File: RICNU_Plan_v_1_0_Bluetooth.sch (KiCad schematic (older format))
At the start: 6 parts, among them SW2 SW_Push, U7 BT121

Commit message: Re-routed CAN, RS-485, and debug connectors (wrong polarity in all)
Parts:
- removed SW2: SW_Push, Buttons_Switches_SMD:SW_SPST_KMR2, symbol SW_Push
- added SW2: SW_Push_4pin, RICNU_Plan_v_1_0:SW_SPST_KMR7, symbol SW_Push_4pin
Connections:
- no-connect marks 20 -> 22
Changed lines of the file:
@@
-$EndComp
-$Comp
-L SW_Push SW2
-U 1 1 59FAF2AD
-P 6900 4500
-F 0 "SW2" H 6950 4600 50  0000 L CNN
-F 1 "SW_Push" H 6900 4440 50  0000 C CNN
-F 2 "Buttons_Switches_SMD:SW_SPST_KMR2" H 6900 4700 50  0001 C CNN
-F 3 "" H 6900 4700 50  0001 C CNN
-	1    6900 4500
-	0    1    1    0
 $EndComp
 $Comp
@@
 Text Label 7100 3450 0    60   ~ 0
 BT_VCC
+$Comp
+L SW_Push_4pin SW2
+U 1 1 5A1F72AC
+P 6900 4500
+F 0 "SW2" H 6950 4600 50  0000 L CNN
+F 1 "SW_Push_4pin" V 7300 4300 50  0001 C CNN
+F 2 "RICNU_Plan_v_1_0:SW_SPST_KMR7" H 6900 4700 50  0001 C CNN
+F 3 "" H 6900 4700 50  0001 C CNN
+	1    6900 4500
+	0    1    1    0
+$EndComp
+NoConn ~ 6800 4300
+NoConn ~ 6800 4700
 $EndSCHEMATC

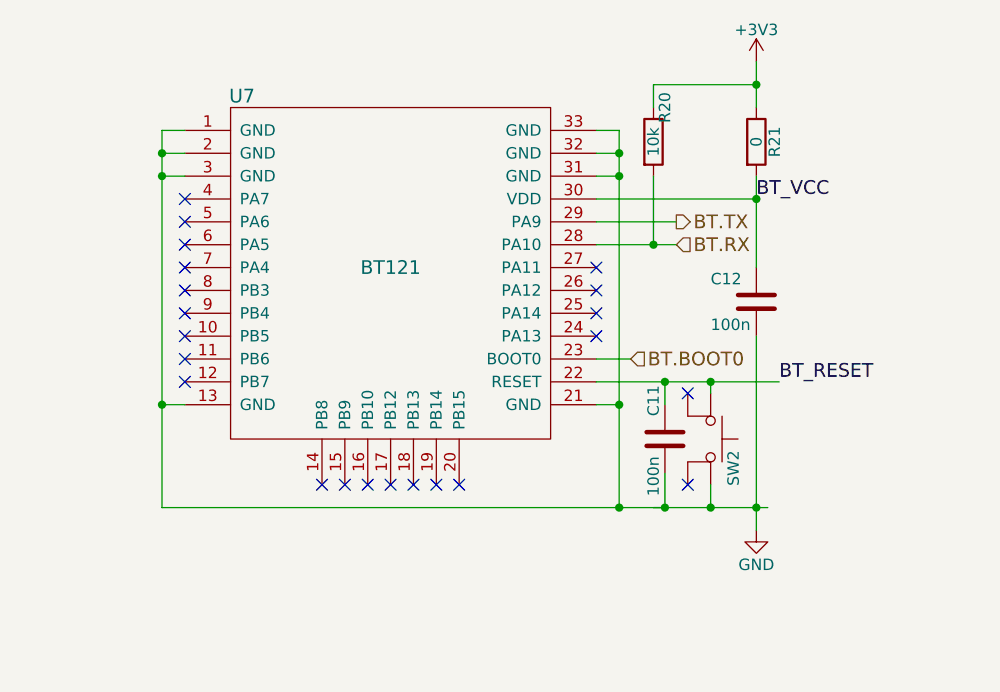
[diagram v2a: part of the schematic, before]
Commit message: Various small changes like comment removal
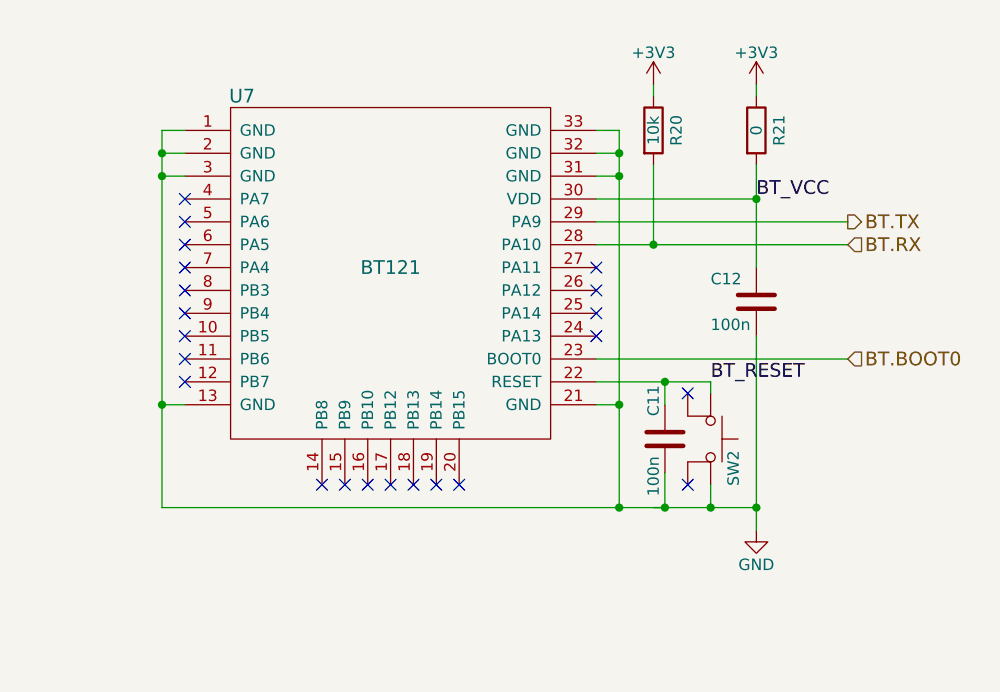
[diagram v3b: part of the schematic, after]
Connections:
- wire segments 27 -> 39
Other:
- moved on the sheet: R20, R21
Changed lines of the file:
@@
 	1    0    0    -1
 $EndComp
-Text HLabel 6550 4150 2    60   Input ~ 0
+Text HLabel 7500 4150 2    60   Input ~ 0
 BT.BOOT0
 $Comp
@@
 	1    0    0    -1
 $EndComp
-Text HLabel 6750 3650 2    60   Input ~ 0
+Text HLabel 7500 3650 2    60   Input ~ 0
 BT.RX
-Text HLabel 6750 3550 2    60   Output ~ 0
+Text HLabel 7500 3550 2    60   Output ~ 0
 BT.TX
 $Comp
 L +3V3 #PWR040
 U 1 1 59FDDC6B
-P 7100 2850
-F 0 "#PWR040" H 7100 2700 50  0001 C CNN
-F 1 "+3V3" H 7100 2990 50  0000 C CNN
-F 2 "" H 7100 2850 50  0001 C CNN
-F 3 "" H 7100 2850 50  0001 C CNN
-	1    7100 2850
+P 7100 2950
+F 0 "#PWR040" H 7100 2800 50  0001 C CNN
+F 1 "+3V3" H 7100 3090 50  0000 C CNN
+F 2 "" H 7100 2950 50  0001 C CNN
+F 3 "" H 7100 2950 50  0001 C CNN
+	1    7100 2950
 	1    0    0    -1
 $EndComp
@@
 L R R21
 U 1 1 59F5F953
-P 7100 3200
-F 0 "R21" V 7180 3200 50  0000 C CNN
-F 1 "0" V 7100 3200 50  0000 C CNN
-F 2 "Resistors_SMD:R_0402_NoSilk" V 7030 3200 50  0001 C CNN
-F 3 "" H 7100 3200 50  0001 C CNN
-	1    7100 3200
+P 7100 3150
+F 0 "R21" V 7200 3150 50  0000 C CNN
+F 1 "0" V 7100 3150 50  0000 C CNN
+F 2 "Resistors_SMD:R_0402_NoSilk" V 7030 3150 50  0001 C CNN
+F 3 "" H 7100 3150 50  0001 C CNN
+	1    7100 3150
 	1    0    0    -1
 $EndComp
@@
 	6900 4800 6900 4700
 Wire Wire Line
-	4500 4800 7150 4800
+	4500 4800 6500 4800
+Wire Wire Line
+	6500 4800 6700 4800
+Wire Wire Line
+	6700 4800 6900 4800
+Wire Wire Line
+	6900 4800 7100 4800
 Wire Wire Line
 	6700 4800 6650 4800
 Connection ~ 6900 4800
-Wire Wire Line
-	6900 4250 6900 4300
 Wire Wire Line
 	6700 4650 6700 4800
@@
 NoConn ~ 5800 4700
 Wire Wire Line
-	4500 3150 4500 4800
+	4500 3150 4500 3250
+Wire Wire Line
+	4500 3250 4500 3350
+Wire Wire Line
+	4500 3350 4500 4350
+Wire Wire Line
+	4500 4350 4500 4800
 Wire Wire Line
 	4500 4350 4600 4350
@@
 	6500 4350 6400 4350
 Wire Wire Line
-	6500 3150 6500 4800
+	6500 3150 6500 3250
+Wire Wire Line
+	6500 3250 6500 3350
+Wire Wire Line
+	6500 3350 6500 4350
+Wire Wire Line
+	6500 4350 6500 4800
 Wire Wire Line
 	6400 3150 6500 3150
@@
 	6400 3450 7100 3450
 Wire Wire Line
-	7100 3350 7100 3750
+	7100 3300 7100 3450
+Wire Wire Line
+	7100 3450 7100 3750
 $Comp
 L GND #PWR041
@@
 $EndComp
 Wire Wire Line
-	7100 4050 7100 4900
+	7100 4050 7100 4800
+Wire Wire Line
+	7100 4800 7100 4900
 Connection ~ 7100 3450
 Wire Wire Line
-	7100 2850 7100 3050
+	7100 2950 7100 3000
 $Comp
 L R R20
 U 1 1 59FBEA73
-P 6650 3200
-F 0 "R20" V 6700 3350 50  0000 C CNN
-F 1 "10k" V 6650 3200 50  0000 C CNN
-F 2 "Resistors_SMD:R_0402_NoSilk" V 6580 3200 50  0001 C CNN
-F 3 "" H 6650 3200 50  0001 C CNN
-	1    6650 3200
-	1    0    0    -1
-$EndComp
-Wire Wire Line
-	6400 3650 6750 3650
-Wire Wire Line
-	6650 3650 6650 3350
+P 6650 3150
+F 0 "R20" V 6750 3150 50  0000 C CNN
+F 1 "10k" V 6650 3150 50  0000 C CNN
+F 2 "Resistors_SMD:R_0402_NoSilk" V 6580 3150 50  0001 C CNN
+F 3 "" H 6650 3150 50  0001 C CNN
+	1    6650 3150
+	1    0    0    -1
+$EndComp
+Wire Wire Line
+	6400 3650 6650 3650
+Wire Wire Line
+	6650 3650 7500 3650
+Wire Wire Line
+	6650 3650 6650 3300
 Connection ~ 7100 4800
 Wire Wire Line
-	6650 3050 6650 2950
-Wire Wire Line
-	6650 2950 7100 2950
-Connection ~ 7100 2950
-Wire Wire Line
-	6400 3550 6750 3550
+	6650 2950 6650 3000
+Wire Wire Line
+	6400 3550 7500 3550
 Connection ~ 6650 3650
 NoConn ~ 4600 3450
@@
 NoConn ~ 6400 3750
 Wire Wire Line
-	6550 4150 6400 4150
-Wire Wire Line
-	6400 4250 7200 4250
-Text Label 7200 4250 0    60   ~ 0
+	7500 4150 6400 4150
+Wire Wire Line
+	6400 4250 6700 4250
+Wire Wire Line
+	6700 4250 6900 4250
+Text Label 6900 4250 0    60   ~ 0
 BT_RESET
-Connection ~ 6900 4250
 Text Label 7100 3450 0    60   ~ 0
 BT_VCC
@@
 NoConn ~ 6800 4300
 NoConn ~ 6800 4700
+Wire Wire Line
+	6900 4250 6900 4300
+$Comp
+L +3V3 #PWR?
+U 1 1 5A70F686
+P 6650 2950
+F 0 "#PWR?" H 6650 2800 50  0001 C CNN
+F 1 "+3V3" H 6650 3090 50  0000 C CNN
+F 2 "" H 6650 2950 50  0001 C CNN
+F 3 "" H 6650 2950 50  0001 C CNN
+	1    6650 2950
+	1    0    0    -1
+$EndComp
 $EndSCHEMATC

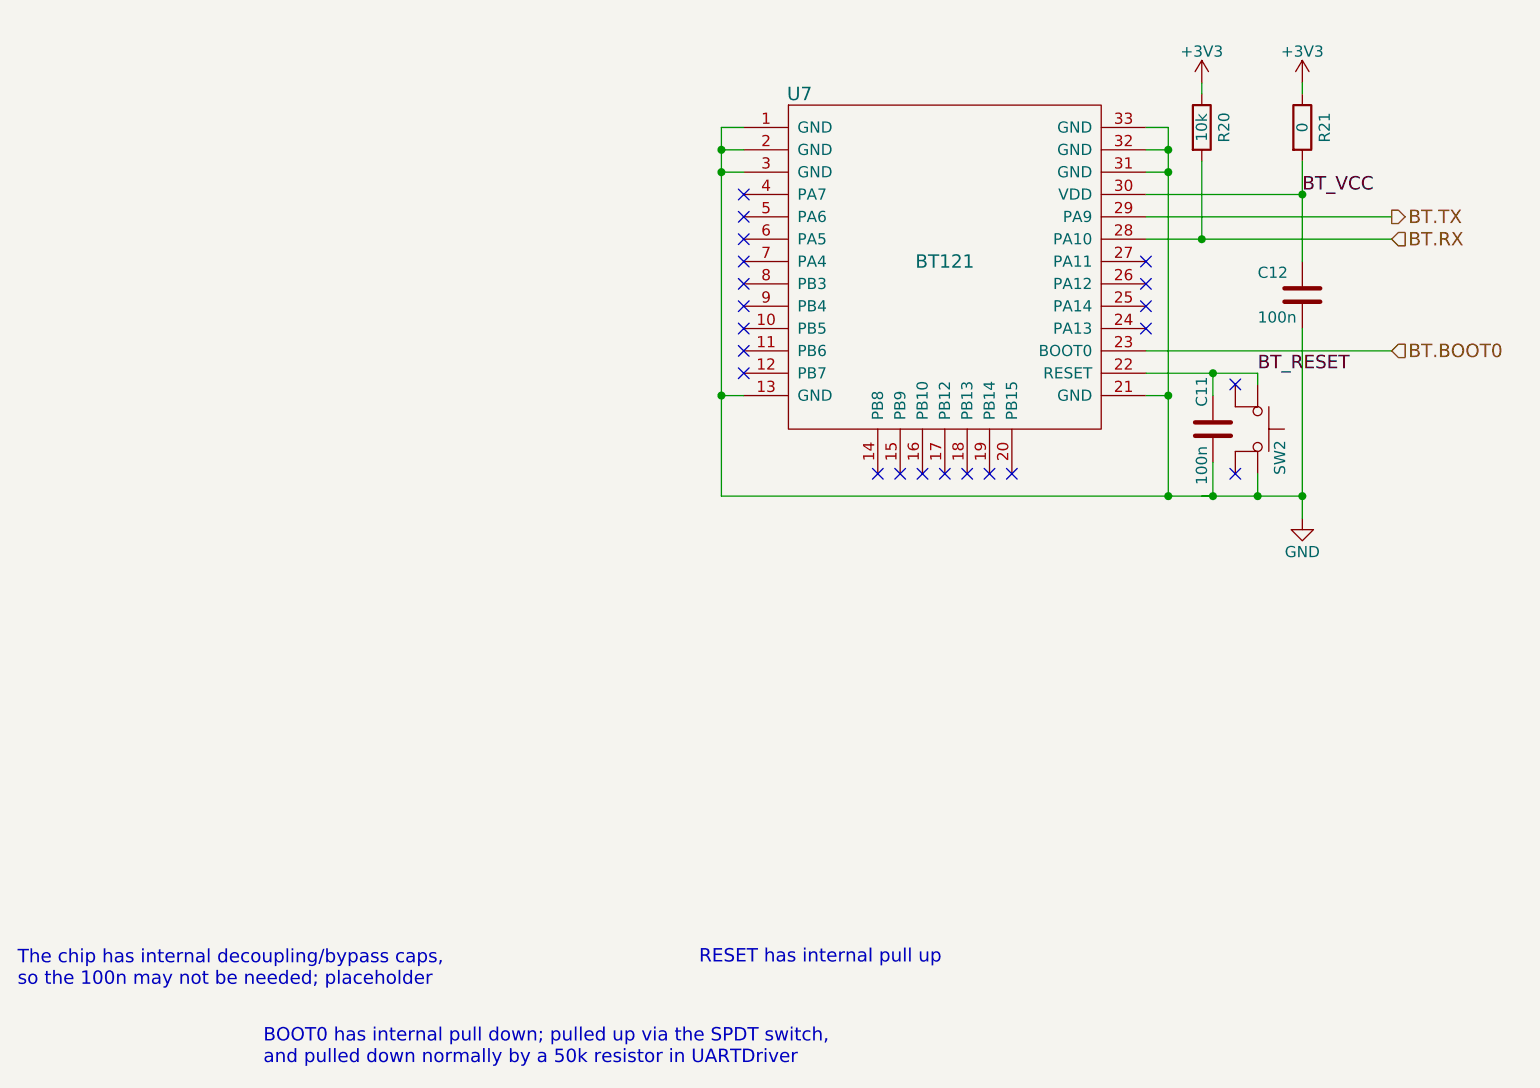
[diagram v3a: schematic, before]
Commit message: Deleting PDFs
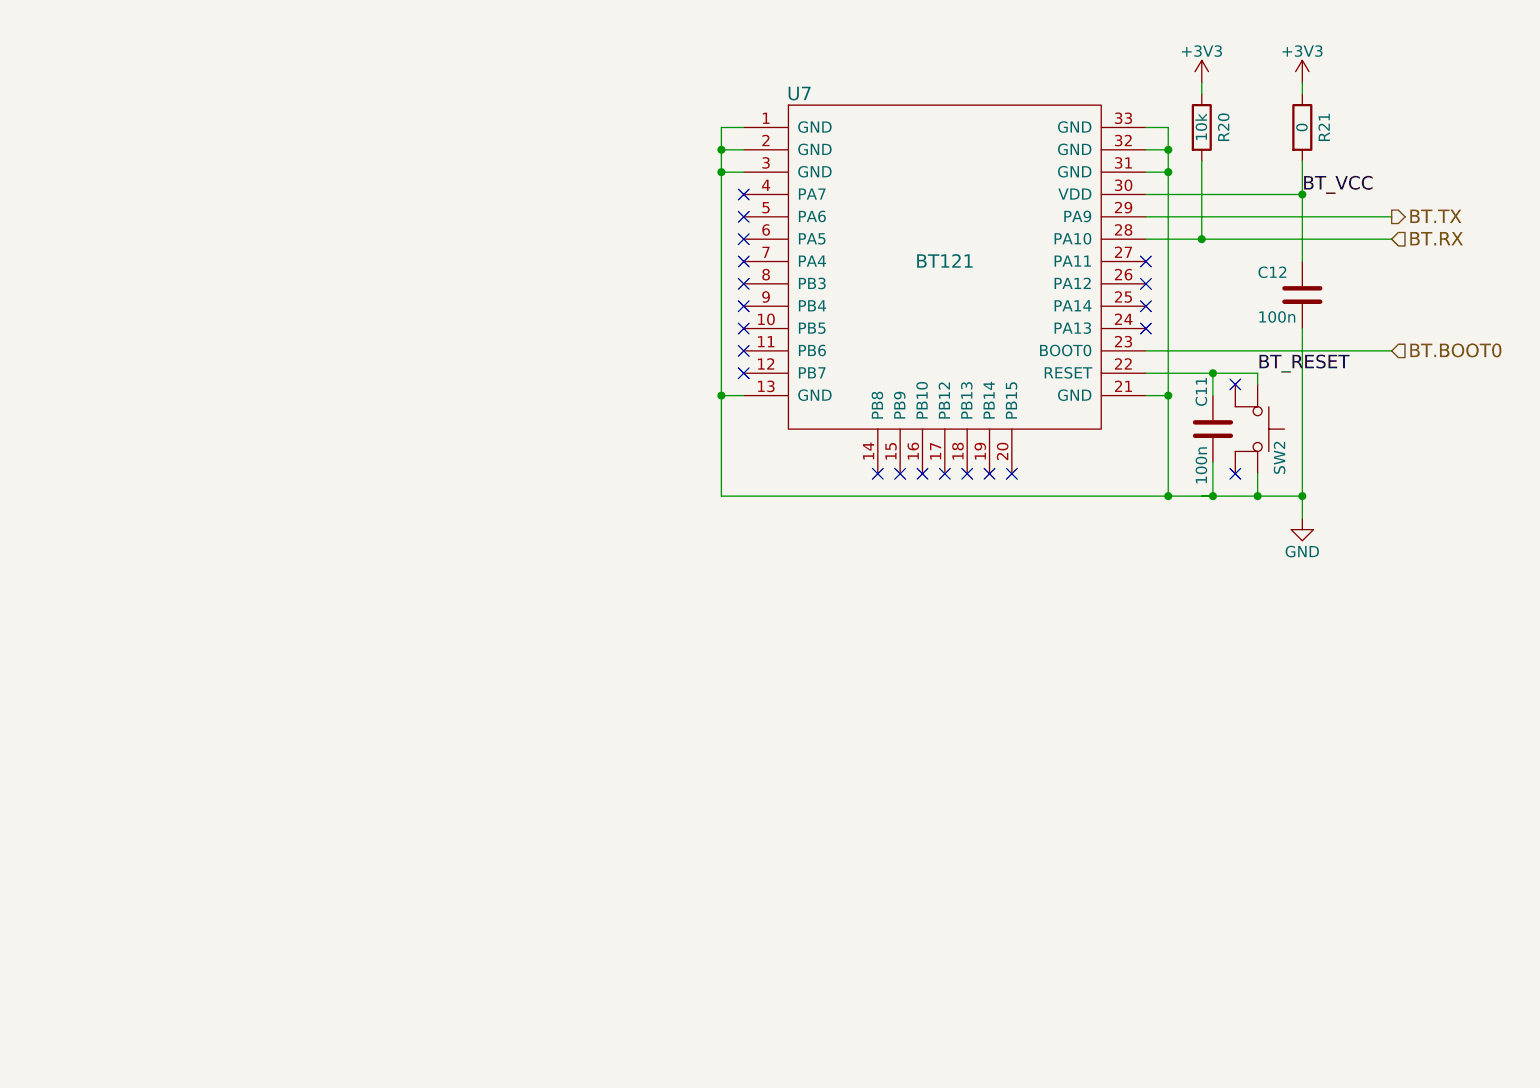
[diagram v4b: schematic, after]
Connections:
- wire segments 39 -> 26
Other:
- note removed: "BOOT0 has internal pull down; pulled up via the SPDT switch, \nand pulled down normally by a 50k resistor in UARTDriver"
- note removed: "RESET has internal pull up"
- note removed: "The chip has internal decoupling/bypass caps, \nso the 100n may not be needed; placeholder"
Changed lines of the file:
@@
 	1    0    0    -1
 $EndComp
-Text Notes 2450 7350 0    60   ~ 0
-BOOT0 has internal pull down; pulled up via the SPDT switch, \nand pulled down normally by a 50k resistor in UARTDriver
-Text Notes 4400 6900 0    60   ~ 0
-RESET has internal pull up
-Text Notes 1350 7000 0    60   ~ 0
-The chip has internal decoupling/bypass caps, \nso the 100n may not be needed; placeholder
 $Comp
 L R R21
@@
 	6900 4800 6900 4700
 Wire Wire Line
-	4500 4800 6500 4800
-Wire Wire Line
-	6500 4800 6700 4800
-Wire Wire Line
-	6700 4800 6900 4800
-Wire Wire Line
-	6900 4800 7100 4800
+	4500 4800 7100 4800
 Wire Wire Line
 	6700 4800 6650 4800
@@
 NoConn ~ 5800 4700
 Wire Wire Line
-	4500 3150 4500 3250
-Wire Wire Line
-	4500 3250 4500 3350
-Wire Wire Line
-	4500 3350 4500 4350
-Wire Wire Line
-	4500 4350 4500 4800
+	4500 3150 4500 4800
 Wire Wire Line
 	4500 4350 4600 4350
@@
 	6500 4350 6400 4350
 Wire Wire Line
-	6500 3150 6500 3250
-Wire Wire Line
-	6500 3250 6500 3350
-Wire Wire Line
-	6500 3350 6500 4350
-Wire Wire Line
-	6500 4350 6500 4800
+	6500 3150 6500 4800
 Wire Wire Line
 	6400 3150 6500 3150
@@
 	6400 3450 7100 3450
 Wire Wire Line
-	7100 3300 7100 3450
-Wire Wire Line
-	7100 3450 7100 3750
+	7100 3300 7100 3750
 $Comp
 L GND #PWR041
@@
 $EndComp
 Wire Wire Line
-	7100 4050 7100 4800
-Wire Wire Line
-	7100 4800 7100 4900
+	7100 4050 7100 4900
 Connection ~ 7100 3450
 Wire Wire Line
@@
 $EndComp
 Wire Wire Line
-	6400 3650 6650 3650
-Wire Wire Line
-	6650 3650 7500 3650
+	6400 3650 7500 3650
 Wire Wire Line
 	6650 3650 6650 3300
@@
 	7500 4150 6400 4150
 Wire Wire Line
-	6400 4250 6700 4250
-Wire Wire Line
-	6700 4250 6900 4250
+	6400 4250 6900 4250
 Text Label 6900 4250 0    60   ~ 0
 BT_RESET
